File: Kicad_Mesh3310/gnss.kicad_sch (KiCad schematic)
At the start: 5 parts, among them U2 NRF9151-LACA-R7

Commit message: Backup work
Adding some extra pads
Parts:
- removed TP14, TP15, TP16, TP17: TestPoint, symbol Connector:TestPoint
- added J3: Sim, mesh3310_footprints:3310_sim, symbol Connector:Conn_01x06_Pin
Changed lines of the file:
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@@
-	)
-	(symbol
-		(lib_id "Connector:TestPoint")
-		(at 48.26 86.36 90)
-		(unit 1)
-		(exclude_from_sim no)
-		(in_bom yes)
-		(on_board yes)
-		(dnp no)
-		(fields_autoplaced yes)
-		(property "Reference" "TP17"
-			(at 44.958 81.28 90)
-			(effects
-				(font
-					(size 1.27 1.27)
-				)
-			)
-		)
-		(property "Value" "TestPoint"
-			(at 44.958 83.82 90)
-			(effects
-				(font
-					(size 1.27 1.27)
-				)
-			)
-		)
-		(property "Footprint" ""
-			(at 48.26 81.28 0)
-			(effects
-				(font
-					(size 1.27 1.27)
-				)
-				(hide yes)
-			)
-		)
-		(property "Datasheet" "~"
-			(at 48.26 81.28 0)
-			(effects
-				(font
-					(size 1.27 1.27)
-				)
-				(hide yes)
-			)
-		)
-		(property "Description" "test point"
-			(at 48.26 86.36 0)
-			(effects
-				(font
-					(size 1.27 1.27)
-				)
-				(hide yes)
-			)
-		)
-		(pin "1"
-		)
-		(instances
-			(project "Mesh3310"
-				(path "/8d65c5ef-7a02-4454-aee5-ab9c49e4aeab/98e1aac4-af48-4762-9c2a-9b5d76c64f4f"
-					(reference "TP17")
-					(unit 1)
-				)
-			)
-		)
-	)
-	(symbol
-		(lib_id "Connector:TestPoint")
-		(at 48.26 81.28 90)
-		(unit 1)
-		(exclude_from_sim no)
-		(in_bom yes)
-		(on_board yes)
-		(dnp no)
-		(fields_autoplaced yes)
-		(property "Reference" "TP15"
-			(at 44.958 76.2 90)
-			(effects
-				(font
-					(size 1.27 1.27)
-				)
-			)
-		)
-		(property "Value" "TestPoint"
-			(at 44.958 78.74 90)
-			(effects
-				(font
-					(size 1.27 1.27)
-				)
-			)
-		)
-		(property "Footprint" ""
-			(at 48.26 76.2 0)
-			(effects
-				(font
-					(size 1.27 1.27)
-				)
-				(hide yes)
-			)
-		)
-		(property "Datasheet" "~"
-			(at 48.26 76.2 0)
-			(effects
-				(font
-					(size 1.27 1.27)
-				)
-				(hide yes)
-			)
-		)
-		(property "Description" "test point"
-			(at 48.26 81.28 0)
-			(effects
-				(font
-					(size 1.27 1.27)
-				)
-				(hide yes)
-			)
-		)
-		(pin "1"
-		)
-		(instances
-			(project "Mesh3310"
-				(path "/8d65c5ef-7a02-4454-aee5-ab9c49e4aeab/98e1aac4-af48-4762-9c2a-9b5d76c64f4f"
-					(reference "TP15")
-					(unit 1)
-				)
-			)
-		)
-	)
-	(symbol
-		(lib_id "Connector:TestPoint")
-		(at 48.26 83.82 90)
-		(unit 1)
-		(exclude_from_sim no)
-		(in_bom yes)
-		(on_board yes)
-		(dnp no)
-		(fields_autoplaced yes)
-		(property "Reference" "TP16"
-			(at 44.958 78.74 90)
-			(effects
-				(font
-					(size 1.27 1.27)
-				)
-			)
-		)
-		(property "Value" "TestPoint"
-			(at 44.958 81.28 90)
-			(effects
-				(font
-					(size 1.27 1.27)
-				)
-			)
-		)
-		(property "Footprint" ""
-			(at 48.26 78.74 0)
-			(effects
-				(font
-					(size 1.27 1.27)
-				)
-				(hide yes)
-			)
-		)
-		(property "Datasheet" "~"
-			(at 48.26 78.74 0)
-			(effects
-				(font
-					(size 1.27 1.27)
-				)
-				(hide yes)
-			)
-		)
-		(property "Description" "test point"
-			(at 48.26 83.82 0)
-			(effects
-				(font
-					(size 1.27 1.27)
-				)
-				(hide yes)
-			)
-		)
-		(pin "1"
-		)
-		(instances
-			(project "Mesh3310"
-				(path "/8d65c5ef-7a02-4454-aee5-ab9c49e4aeab/98e1aac4-af48-4762-9c2a-9b5d76c64f4f"
-					(reference "TP16")
-					(unit 1)
-				)
-			)
-		)
-	)
-	(symbol
-		(lib_id "Connector:TestPoint")
-		(at 48.26 78.74 90)
-		(unit 1)
-		(exclude_from_sim no)
-		(in_bom yes)
-		(on_board yes)
-		(dnp no)
-		(fields_autoplaced yes)
-		(property "Reference" "TP14"
-			(at 44.958 73.66 90)
-			(effects
-				(font
-					(size 1.27 1.27)
-				)
-			)
-		)
-		(property "Value" "TestPoint"
-			(at 44.958 76.2 90)
-			(effects
-				(font
-					(size 1.27 1.27)
-				)
-			)
-		)
-		(property "Footprint" ""
-			(at 48.26 73.66 0)
-			(effects
-				(font
-					(size 1.27 1.27)
-				)
-				(hide yes)
-			)
-		)
-		(property "Datasheet" "~"
-			(at 48.26 73.66 0)
-			(effects
-				(font
-					(size 1.27 1.27)
-				)
-				(hide yes)
-			)
-		)
-		(property "Description" "test point"
-			(at 48.26 78.74 0)
-			(effects
-				(font
-					(size 1.27 1.27)
-				)
-				(hide yes)
-			)
-		)
-		(pin "1"
-		)
-		(instances
-			(project "Mesh3310"
-				(path "/8d65c5ef-7a02-4454-aee5-ab9c49e4aeab/98e1aac4-af48-4762-9c2a-9b5d76c64f4f"
-					(reference "TP14")
-					(unit 1)
-				)
-			)
-		)
 	)
 	(symbol
@@
 					(unit 1)
 				)
+			)
+		)
+	)
+	(symbol
+		(lib_id "Connector:Conn_01x06_Pin")
+		(at 33.02 81.28 0)
+		(unit 1)
+		(exclude_from_sim no)
+		(in_bom yes)
+		(on_board yes)
+		(dnp no)
+		(fields_autoplaced yes)
+		(property "Reference" "J3"
+			(at 33.655 71.12 0)
+			(effects
+				(font
+					(size 1.27 1.27)
+				)
+			)
+		)
+		(property "Value" "Sim"
+			(at 33.655 73.66 0)
+			(effects
+				(font
+					(size 1.27 1.27)
+				)
+			)
+		)
+		(property "Footprint" "mesh3310_footprints:3310_sim"
+			(at 33.02 81.28 0)
+			(effects
+				(font
+					(size 1.27 1.27)
+				)
+				(hide yes)
+			)
+		)
+		(property "Datasheet" "~"
+			(at 33.02 81.28 0)
+			(effects
+				(font
+					(size 1.27 1.27)
+				)
+				(hide yes)
+			)
+		)
+		(property "Description" "Generic connector, single row, 01x06, script generated"
+			(at 33.02 81.28 0)
+			(effects
+				(font
+					(size 1.27 1.27)
+				)
+				(hide yes)
+			)
+		)
+		(pin "5"
+		)
+		(pin "4"
+		)
+		(pin "3"
+		)
+		(pin "1"
+		)
+		(pin "6"
+		)
+		(pin "2"
+		)
+		(instances
+			(project "Mesh3310"
+				(path "/8d65c5ef-7a02-4454-aee5-ab9c49e4aeab/98e1aac4-af48-4762-9c2a-9b5d76c64f4f"
+					(reference "J3")
+					(unit 1)
+				)

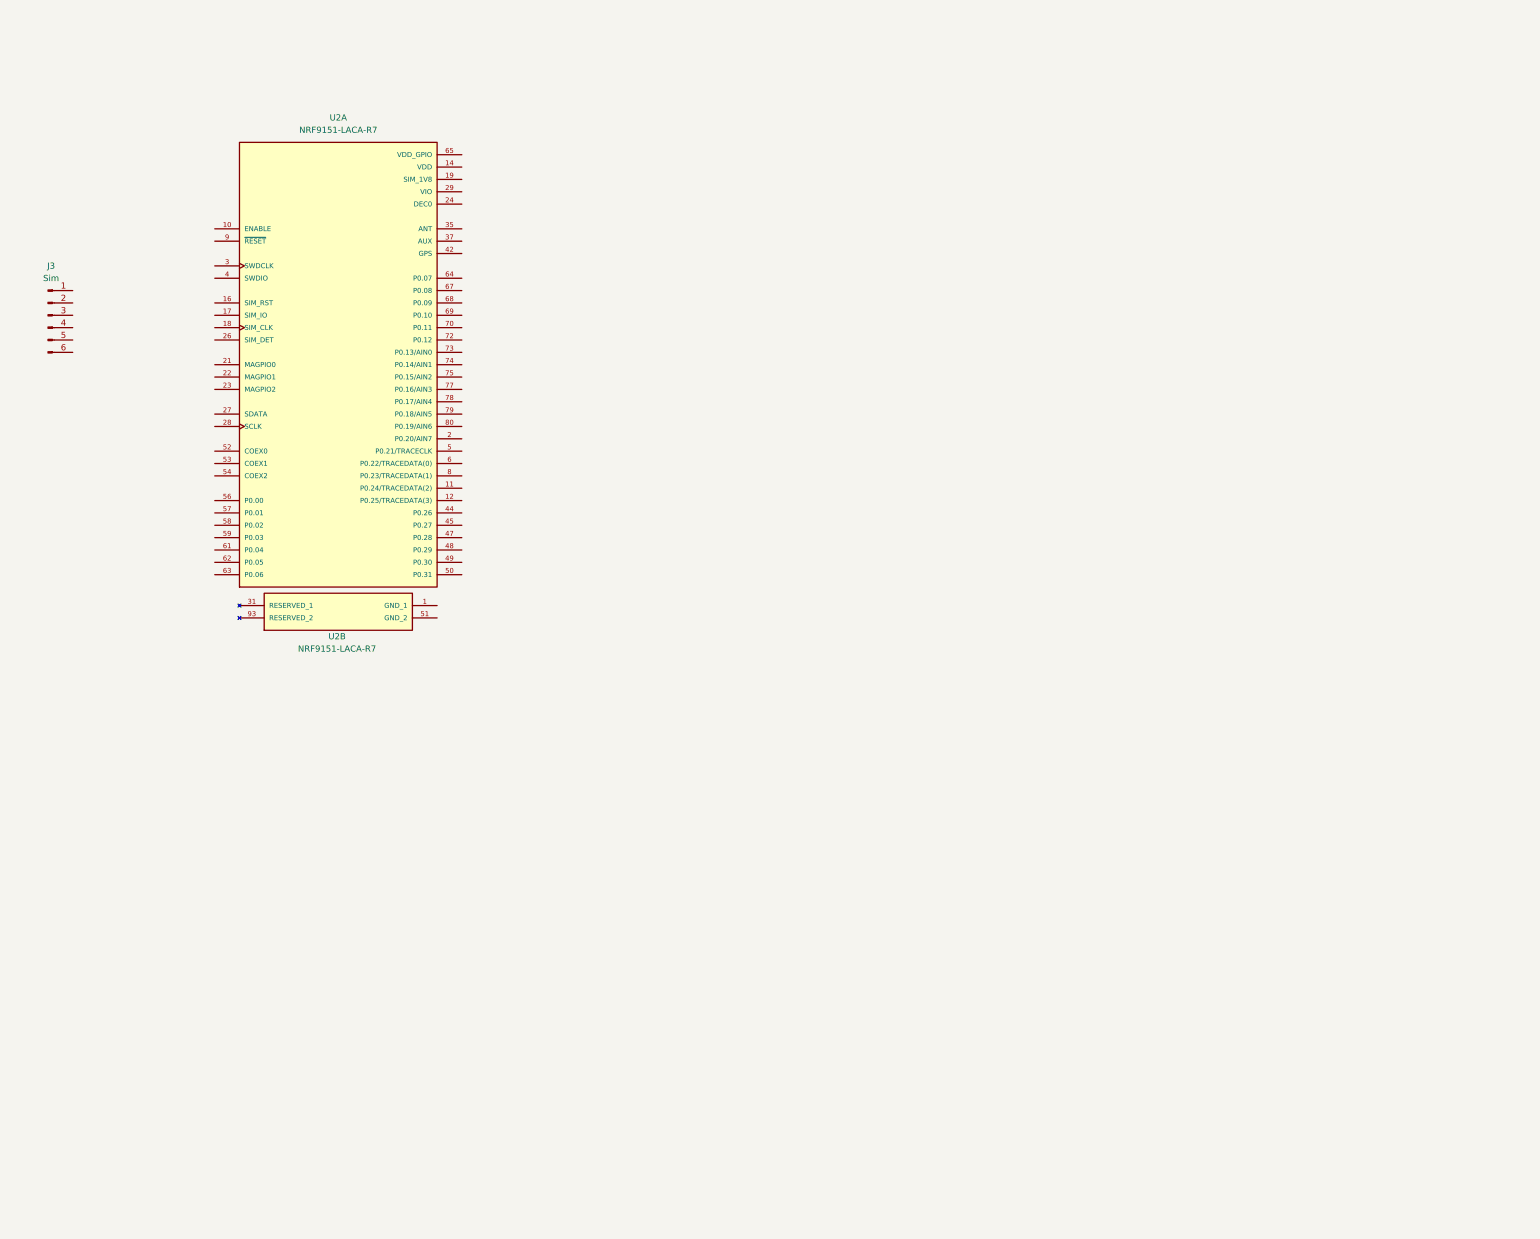
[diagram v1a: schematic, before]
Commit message: Schematic changes
Adding gsm module , interfaces : mic+earspeaker
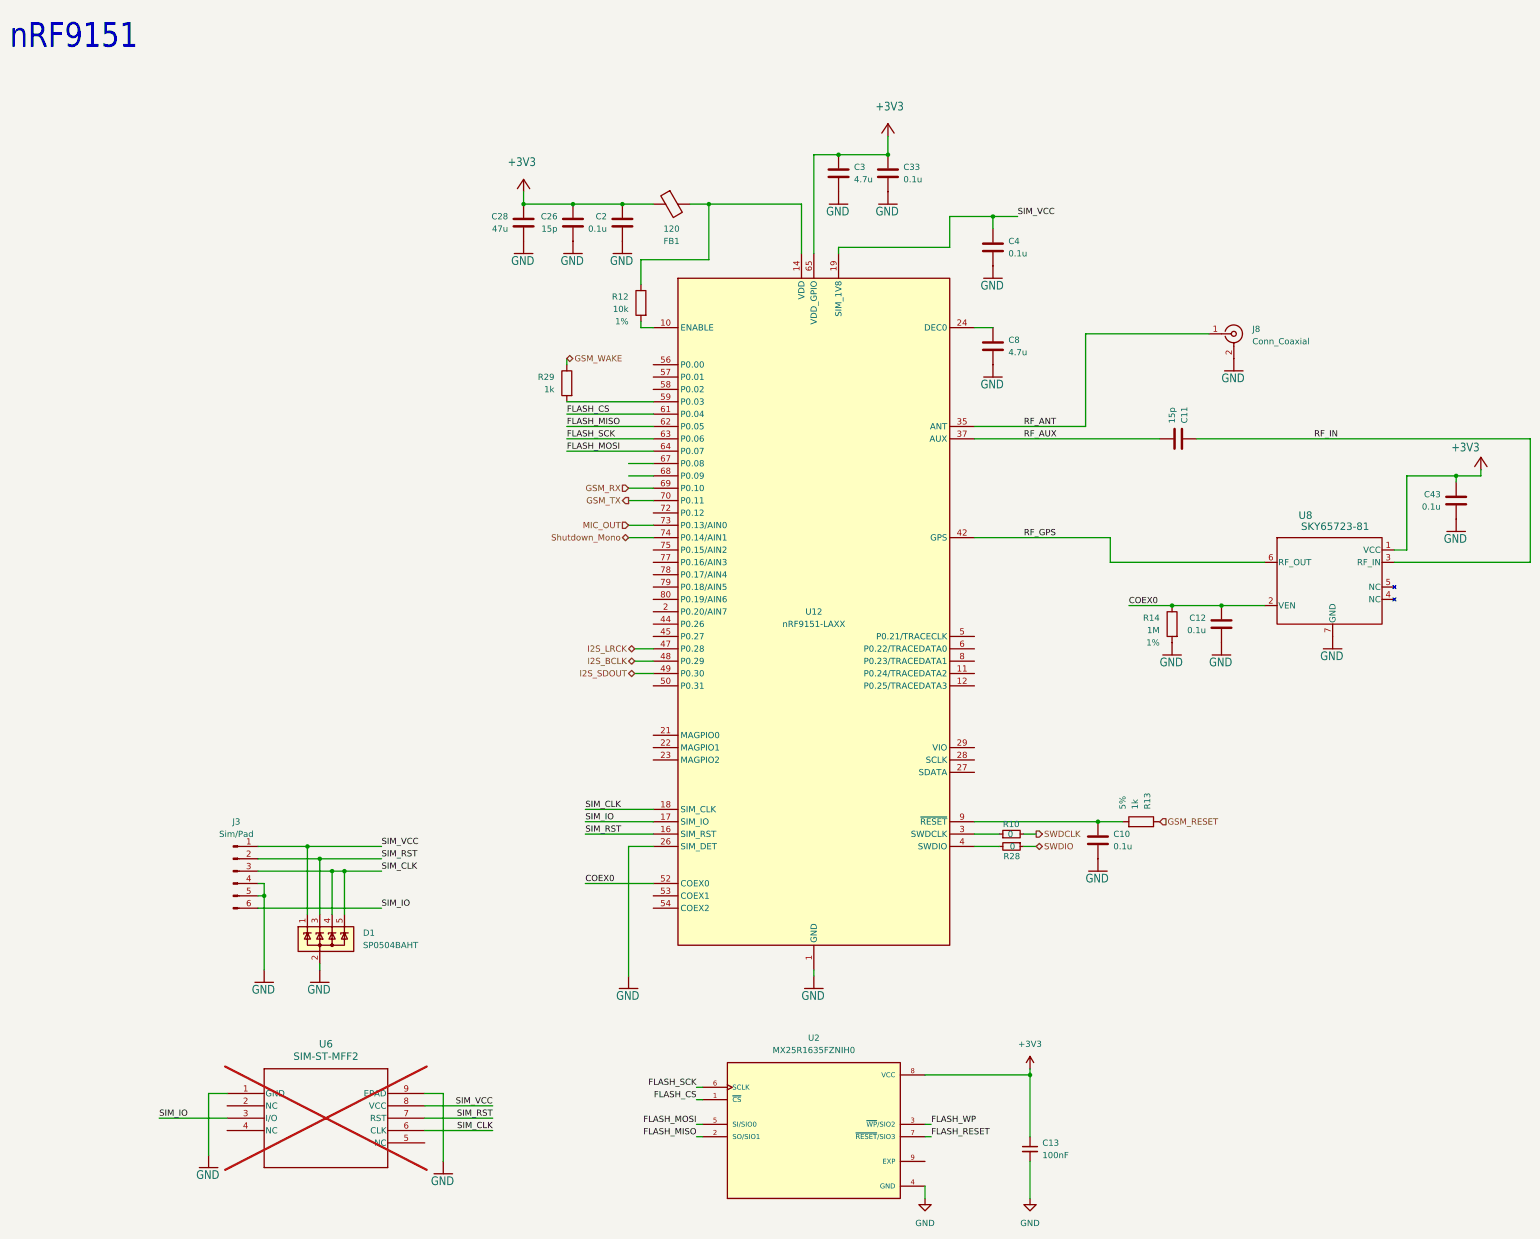
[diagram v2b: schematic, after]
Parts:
- removed U2: NRF9151-LACA-R7, mesh3310_footprints:XCVR_NRF9151-LACA-R7, symbol NRF9151-LACA-R7:NRF9151-LACA-R7
- added C10, C12, C2, C4: 0.1u, Resistor_SMD:R_0201_0603Metric, symbol Device:C
- added C11: 15p, Resistor_SMD:R_0201_0603Metric, symbol Device:C
- added C13: 100nF, Capacitor_SMD:C_0201_0603Metric, symbol Device:C_Small
- added C26: 15p, Capacitor_SMD:C_0201_0603Metric, symbol Device:C
- added C28: 47u, Capacitor_SMD:C_0201_0603Metric, symbol Device:C
- added C3: 4.7u, Resistor_SMD:R_0201_0603Metric, symbol Device:C
- added C33, C43: 0.1u, Capacitor_SMD:C_0201_0603Metric, symbol Device:C
- added C8: 4.7u, Capacitor_SMD:C_0201_0603Metric, symbol Device:C
- added D1: SP0504BAHT, Package_TO_SOT_SMD:SOT-23-5, symbol Power_Protection:SP0504BAHT
- added FB1: 120, Resistor_SMD:R_0201_0603Metric, symbol Device:FerriteBead
- added J8: Conn_Coaxial, Connector_Coaxial:U.FL_Hirose_U.FL-R-SMT-1_Vertical, symbol Connector:Conn_Coaxial
- added R10, R28: 0, Resistor_SMD:R_0201_0603Metric, symbol Device:R_Small
- added R12: 10k, Resistor_SMD:R_0201_0603Metric, symbol Device:R
- added R13, R29: 1k, Resistor_SMD:R_0201_0603Metric, symbol Device:R
- added R14: 1M, Resistor_SMD:R_0201_0603Metric, symbol Device:R
- added U12: nRF9151-LAXX, mesh3310_footprints:XCVR_NRF9151-LACA-R7, symbol PCM_nordic-lib-kicad-nrf9:nRF9151-LAXX
- added U2: MX25R1635FZNIH0, mesh3310_footprints:SON127P500X600X80-9N, symbol MX25R1635FZNIH0:MX25R1635FZNIH0
- added U6: SIM-ST-MFF2, mesh3310_footprints:PSON127P500X600X82-9N, symbol 2024-04-08_13-26-58:SIM-ST-MFF2
- added U8: SKY65723-81, mesh3310_footprints:SKY65723-81, symbol 2024-04-10_15-11-21:SKY65723-81
- J3: value Sim -> Sim/Pad
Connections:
- net SIM_VCC: now reaches J3.1 (Pin_1)
- net SIM_VCC: now also C4.1, D1.1 (K), U12.19 (SIM_1V8), U6.8 (VCC)
- net SIM_RST: now reaches J3.2 (Pin_2)
- net SIM_RST: now also D1.3 (K), U12.16 (SIM_RST), U6.7 (RST)
- net SIM_CLK: now reaches J3.3 (Pin_3)
- net SIM_CLK: now also D1.4 (K), D1.5 (K), U12.18 (SIM_CLK), U6.6 (CLK)
- net GND: now reaches J3.4 (Pin_4)
- net GND: now also J3.5 (Pin_5), C10.2, C12.2, C13.2, C2.2, C26.2, C28.2, C3.2, C33.2, C4.2, C43.2, C8.2, D1.2 (A), J8.2 (Ext), R14.2, U12.1 (GND), U12.105 (GND), U12.106 (GND), U12.107 (GND), U12.108 (GND), U12.109 (GND), U12.110 (GND), U12.111 (GND), U12.112 (GND), U12.113 (GND), U12.13 (GND), U12.15 (GND), U12.20 (GND), U12.25 (GND), U12.26 (SIM_DET), U12.30 (GND), U12.34 (GND), U12.36 (GND), U12.38 (GND), U12.39 (GND), U12.40 (GND), U12.41 (GND), U12.43 (GND), U12.46 (GND), U12.51 (GND), U12.55 (GND), U12.60 (GND), U12.66 (GND), U12.7 (GND), U12.71 (GND), U12.76 (GND), U2.4 (GND), U6.1 (GND), U6.9 (EPAD), U8.7 (GND)
- net SIM_IO: now reaches J3.6 (Pin_6)
- net SIM_IO: now also U12.17 (SIM_IO), U6.3 (I/O)
- new net: R29.2, U12.59 (P0.03)
- new net: C8.1, U12.24 (DEC0)
- new net: R12.2, U12.10 (ENABLE)
- new net: FB1.2, R12.1, U12.14 (VDD)
- new net: R10.1, U12.3 (SWDCLK)
- new net: R28.2, U12.4 (SWDIO)
- new net: C10.1, R13.2, U12.9 (~{RESET})
- new net +3V3: C13.1, C2.1, C26.1, C28.1, C3.1, C33.1, C43.1, FB1.1, U12.65 (VDD_GPIO), U2.8 (VCC), U8.1 (VCC)
- new net COEX0: C12.1, R14.1, U12.52 (COEX0), U8.2 (VEN)
- new net FLASH_CS: U12.61 (P0.04), U2.1 (~{CS})
- new net FLASH_MISO: U12.62 (P0.05), U2.2 (SO/SIO1)
- new net FLASH_MOSI: U12.64 (P0.07), U2.5 (SI/SIO0)
- new net FLASH_RESET: U2.7 (~{RESET}/SIO3)
- new net FLASH_SCK: U12.63 (P0.06), U2.6 (SCLK)
- new net FLASH_WP: U2.3 (~{WP}/SIO2)
- new net GSM_RESET: R13.1
- new net GSM_RX: U12.69 (P0.10)
- new net GSM_TX: U12.70 (P0.11)
- new net GSM_WAKE: R29.1
- new net I2S_BCLK: U12.48 (P0.29)
- new net I2S_LRCK: U12.47 (P0.28)
- new net I2S_SDOUT: U12.49 (P0.30)
- new net MIC_OUT: U12.73 (P0.13/AIN0)
- new net RF_ANT: J8.1 (In), U12.35 (ANT)
- new net RF_AUX: C11.2, U12.37 (AUX)
- new net RF_GPS: U12.42 (GPS), U8.6 (RF_OUT)
- new net RF_IN: C11.1, U8.3 (RF_IN)
- new net SWDCLK: R10.2
- new net SWDIO: R28.1
- new net Shutdown_Mono: U12.74 (P0.14/AIN1)
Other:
- note added: "nRF9151"
- moved on the sheet: J3
